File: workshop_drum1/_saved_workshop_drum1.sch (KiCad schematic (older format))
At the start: 40 parts, among them J1 9v_Battery_Clip, J2 Trigger_Input, J3 Output, U1 LM358, U2 7414, U3 78L05

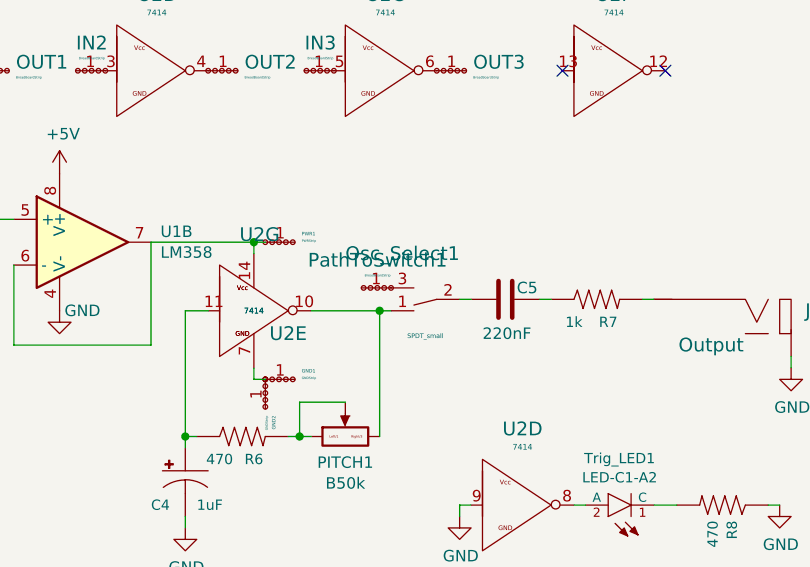
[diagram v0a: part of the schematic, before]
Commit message: got rid of square pins - printed gerbers - changed names- relayed traces
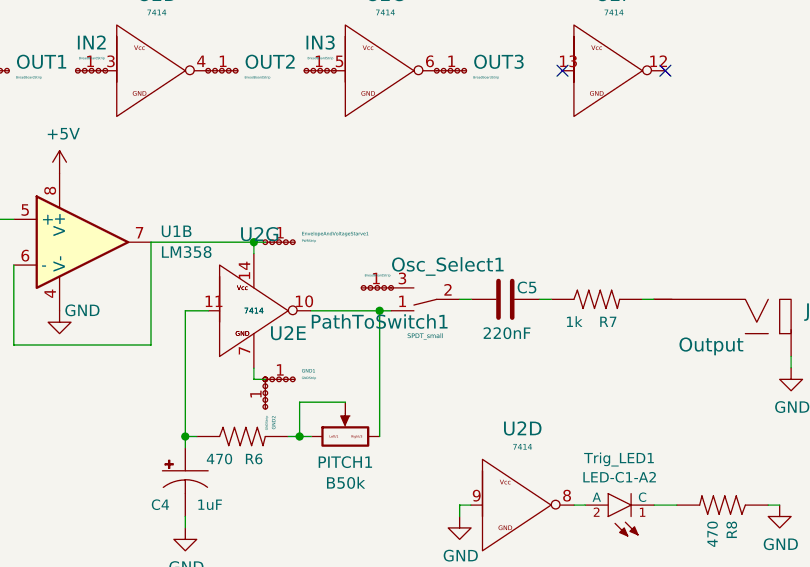
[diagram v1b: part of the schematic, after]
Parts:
- renumbered PWR1 to EnvelopeAndVoltageStarve1
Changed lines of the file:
@@
 U 1 1 5A3358B6
 P 5700 1900
-F 0 "Osc_Select1" H 5800 1700 60  0000 C CNN
+F 0 "Osc_Select1" H 5600 1750 60  0000 C CNN
 F 1 "SPDT_small" H 5700 2060 20  0000 C CNN
 F 2 "zfoot:SPDT_Wired" H 5700 1900 60  0001 C CNN
@@
 U 1 1 5A33DD61
 P 5550 1850
-F 0 "PathToSwitch1" H 5609 1729 60  0000 C CNN
+F 0 "PathToSwitch1" H 5600 2000 60  0000 C CNN
 F 1 "BreadBoardStrip" H 5609 1795 10  0000 C CNN
 F 2 "zfoot:BreadBoardStrip_4" H 5420 1830 60  0001 C CNN
@@
 $EndComp
 $Comp
-L GNDStrip PWR1
+L GNDStrip EnvelopeAndVoltageStarve1
 U 1 1 5A330F13
 P 5000 1650
-F 0 "PWR1" H 5159 1687 15  0000 L CNN
+F 0 "EnvelopeAndVoltageStarve1" H 5159 1687 15  0000 L CNN
 F 1 "PWRStrip" H 5159 1656 10  0000 L CNN
 F 2 "zfoot:BreadBoardStrip_4" H 4870 1630 60  0001 C CNN
